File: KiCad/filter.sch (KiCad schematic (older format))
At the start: 26 parts

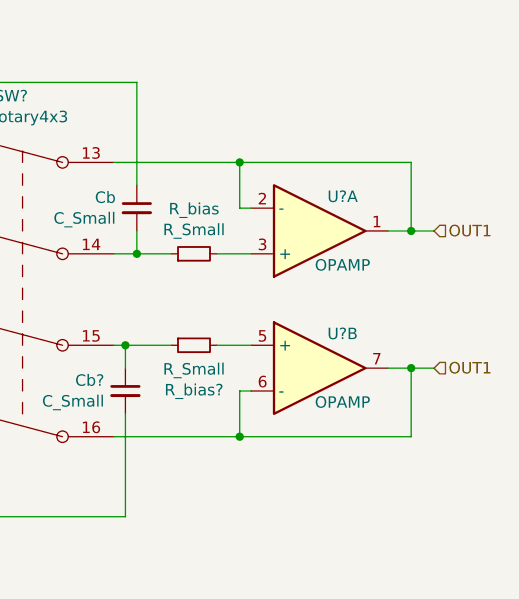
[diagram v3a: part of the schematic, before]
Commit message: removed VU Meter sheet
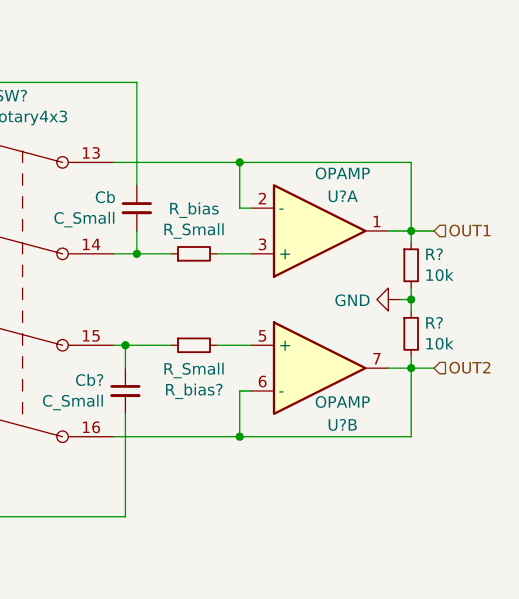
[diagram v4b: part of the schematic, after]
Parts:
- added R? (x2): 10k, symbol Device:R_Small
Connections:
- net GND: now also R?.1, R?.2
- net OUT1: now also R?.1; no longer SW?.16, U?.6 (-), U?.7
- new net OUT2: R?.2, SW?.16, U?.6 (-), U?.7
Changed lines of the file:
@@
 $Descr A4 11693 8268
 encoding utf-8
-Sheet 2 5
+Sheet 4 6
 Title ""
 Date ""
@@
 P 7300 3700
 F 0 "U?" H 7400 3550 50  0000 C CNN
-F 1 "OPAMP" H 7400 3850 50  0000 C CNN
+F 1 "OPAMP" H 7400 3450 50  0000 C CNN
 F 2 "" H 7300 3700 50  0001 C CNN
 F 3 "~" H 7300 3700 50  0001 C CNN
@@
 U 2 1 6049958E
 P 7300 4300
-F 0 "U?" H 7400 4450 50  0000 C CNN
+F 0 "U?" H 7400 4050 50  0000 C CNN
 F 1 "OPAMP" H 7400 4150 50  0000 C CNN
 F 2 "" H 7300 4300 50  0001 C CNN
@@
 	4700 4300 4450 4300
 Text HLabel 7800 4300 2    50   Input ~ 0
-OUT1
+OUT2
 Wire Wire Line
 	7700 4300 7600 4300
@@
 Wire Wire Line
 	4000 4950 4150 4950
+$Comp
+L Device:R_Small R?
+U 1 1 60598110
+P 7700 3850
+F 0 "R?" H 7759 3896 50  0000 L CNN
+F 1 "10k" H 7759 3805 50  0000 L CNN
+F 2 "" H 7700 3850 50  0001 C CNN
+F 3 "~" H 7700 3850 50  0001 C CNN
+	1    7700 3850
+	1    0    0    -1
+$EndComp
+$Comp
+L Device:R_Small R?
+U 1 1 60598B9D
+P 7700 4150
+F 0 "R?" H 7759 4196 50  0000 L CNN
+F 1 "10k" H 7759 4105 50  0000 L CNN
+F 2 "" H 7700 4150 50  0001 C CNN
+F 3 "~" H 7700 4150 50  0001 C CNN
+	1    7700 4150
+	1    0    0    -1
+$EndComp
+Wire Wire Line
+	7700 4250 7700 4300
+Wire Wire Line
+	7700 3750 7700 3700
+Wire Wire Line
+	7700 3950 7700 4000
+$Comp
+L power:GND #PWR?
+U 1 1 6059E0F8
+P 7650 4000
+F 0 "#PWR?" H 7650 3750 50  0001 C CNN
+F 1 "GND" V 7655 3872 50  0000 R CNN
+F 2 "" H 7650 4000 50  0001 C CNN
+F 3 "" H 7650 4000 50  0001 C CNN
+	1    7650 4000
+	0    1    1    0
+$EndComp
+Wire Wire Line
+	7650 4000 7700 4000
+Connection ~ 7700 4000
+Wire Wire Line
+	7700 4000 7700 4050
 $EndSCHEMATC

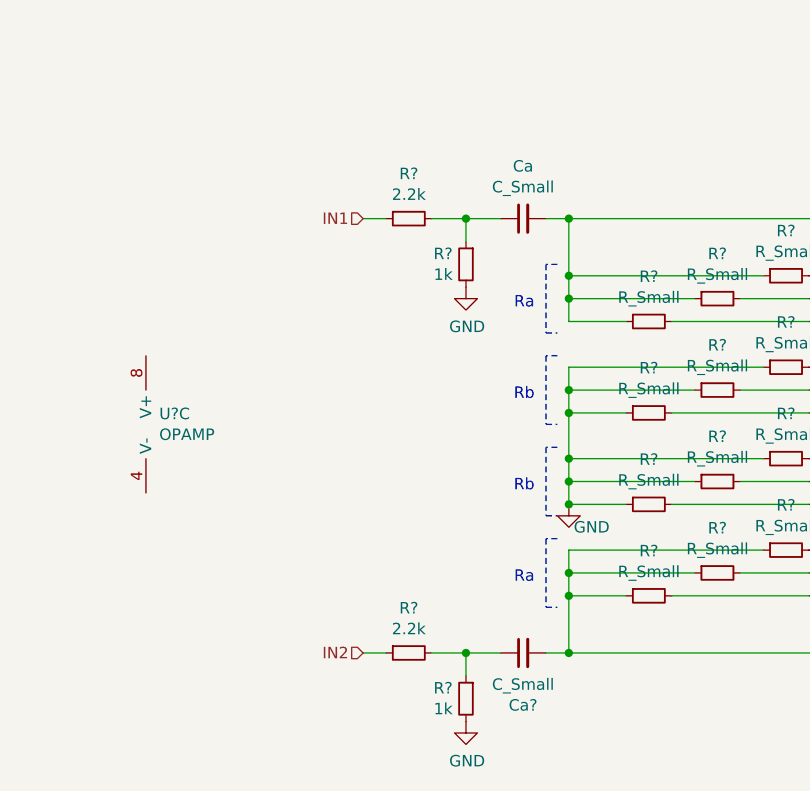
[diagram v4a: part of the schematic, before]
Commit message: changed 4053 to DG419 & added negative latch
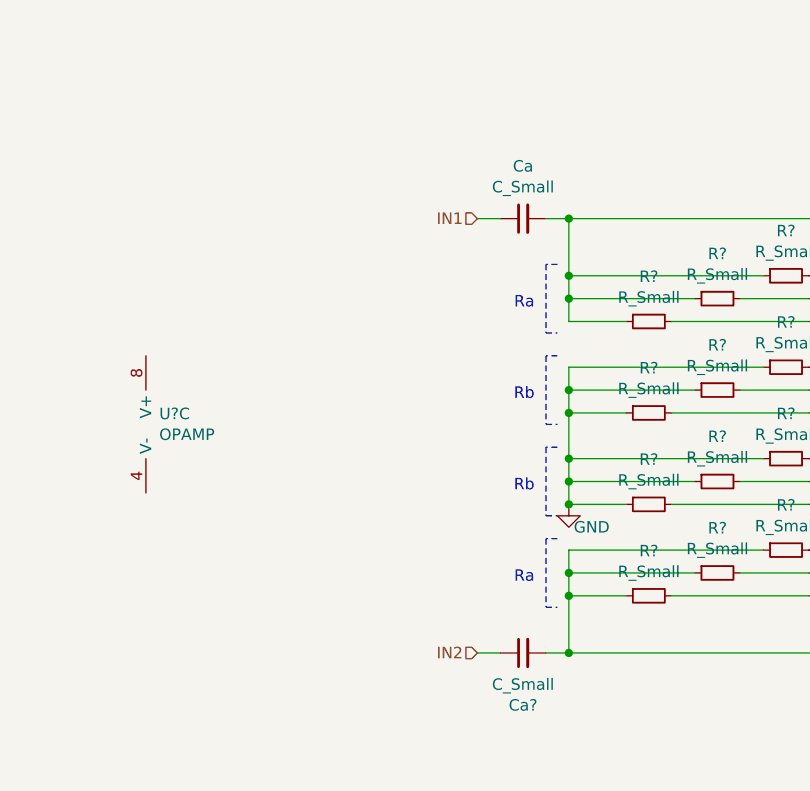
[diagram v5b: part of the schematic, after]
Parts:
- removed R? (x2): 2.2k, symbol Device:R_Small
- removed R? (x2): 1k, symbol Device:R_Small
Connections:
- net IN1: now also Ca.1
- net IN2: now also Ca?.1
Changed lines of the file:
@@
 $Descr A4 11693 8268
 encoding utf-8
-Sheet 4 6
+Sheet 3 8
 Title ""
 Date ""
@@
 Text HLabel 7800 3700 2    50   Input ~ 0
 OUT1
-Text HLabel 3550 3050 0    50   Input ~ 0
+Text HLabel 4050 3050 0    50   Input ~ 0
 IN1
 $Comp
@@
 Wire Wire Line
 	4350 4950 4450 4950
-Text HLabel 3550 4950 0    50   Input ~ 0
+Text HLabel 4050 4950 0    50   Input ~ 0
 IN2
 Wire Notes Line style solid
@@
 	6950 3400 6400 3400
 Connection ~ 6950 3400
-$Comp
-L Device:R_Small R?
-U 1 1 60412BF2
-P 3750 3050
-F 0 "R?" V 3554 3050 50  0000 C CNN
-F 1 "2.2k" V 3645 3050 50  0000 C CNN
-F 2 "" H 3750 3050 50  0001 C CNN
-F 3 "~" H 3750 3050 50  0001 C CNN
-	1    3750 3050
-	0    -1   1    0
-$EndComp
-Wire Wire Line
-	3650 3050 3550 3050
-Wire Wire Line
-	3850 3050 4000 3050
-$Comp
-L Device:R_Small R?
-U 1 1 60415A9E
-P 4000 3250
-F 0 "R?" H 4058 3296 50  0000 L CNN
-F 1 "1k" H 4058 3205 50  0000 L CNN
-F 2 "" H 4000 3250 50  0001 C CNN
-F 3 "~" H 4000 3250 50  0001 C CNN
-	1    4000 3250
-	-1   0    0    -1
-$EndComp
-Wire Wire Line
-	4000 3150 4000 3050
-Connection ~ 4000 3050
-Wire Wire Line
-	4000 3050 4150 3050
-$Comp
-L power:GND #PWR?
-U 1 1 6041757F
-P 4000 3350
-F 0 "#PWR?" H 4000 3100 50  0001 C CNN
-F 1 "GND" H 4005 3177 50  0000 C CNN
-F 2 "" H 4000 3350 50  0001 C CNN
-F 3 "" H 4000 3350 50  0001 C CNN
-	1    4000 3350
-	1    0    0    -1
-$EndComp
-$Comp
-L Device:R_Small R?
-U 1 1 60418D58
-P 3750 4950
-F 0 "R?" V 3554 4950 50  0000 C CNN
-F 1 "2.2k" V 3645 4950 50  0000 C CNN
-F 2 "" H 3750 4950 50  0001 C CNN
-F 3 "~" H 3750 4950 50  0001 C CNN
-	1    3750 4950
-	0    -1   1    0
-$EndComp
-Wire Wire Line
-	3650 4950 3550 4950
-Wire Wire Line
-	3850 4950 4000 4950
-$Comp
-L Device:R_Small R?
-U 1 1 60418D60
-P 4000 5150
-F 0 "R?" H 4058 5196 50  0000 L CNN
-F 1 "1k" H 4058 5105 50  0000 L CNN
-F 2 "" H 4000 5150 50  0001 C CNN
-F 3 "~" H 4000 5150 50  0001 C CNN
-	1    4000 5150
-	-1   0    0    -1
-$EndComp
-Wire Wire Line
-	4000 5050 4000 4950
-Connection ~ 4000 4950
-$Comp
-L power:GND #PWR?
-U 1 1 60418D69
-P 4000 5250
-F 0 "#PWR?" H 4000 5000 50  0001 C CNN
-F 1 "GND" H 4005 5077 50  0000 C CNN
-F 2 "" H 4000 5250 50  0001 C CNN
-F 3 "" H 4000 5250 50  0001 C CNN
-	1    4000 5250
-	1    0    0    -1
-$EndComp
-Wire Wire Line
-	4000 4950 4150 4950
 $Comp
 L Device:R_Small R?
@@
 Wire Wire Line
 	7700 4000 7700 4050
+Wire Wire Line
+	4050 3050 4150 3050
+Wire Wire Line
+	4050 4950 4150 4950
 $EndSCHEMATC
